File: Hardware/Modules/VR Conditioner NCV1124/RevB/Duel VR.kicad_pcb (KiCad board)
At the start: 2 copper layers, 24 x 22.4 mm, 15 parts, among them IC1 NCV1124, J3 Speedy VR Mount

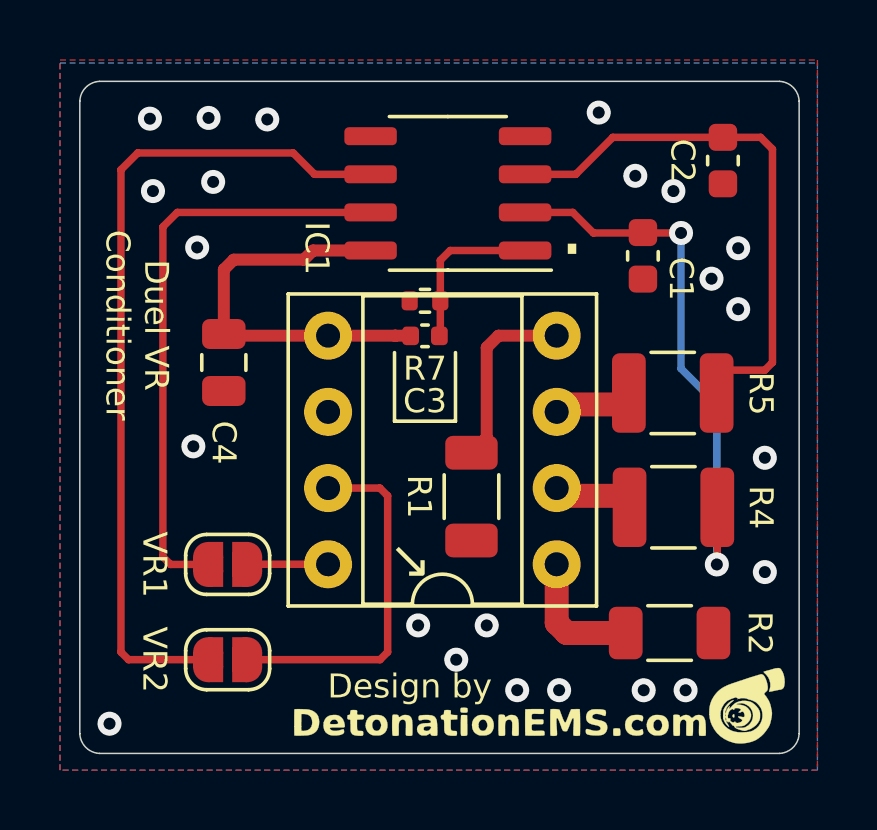
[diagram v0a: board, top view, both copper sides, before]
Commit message: VRNCV-B
Layout update. Schematic unchanged.
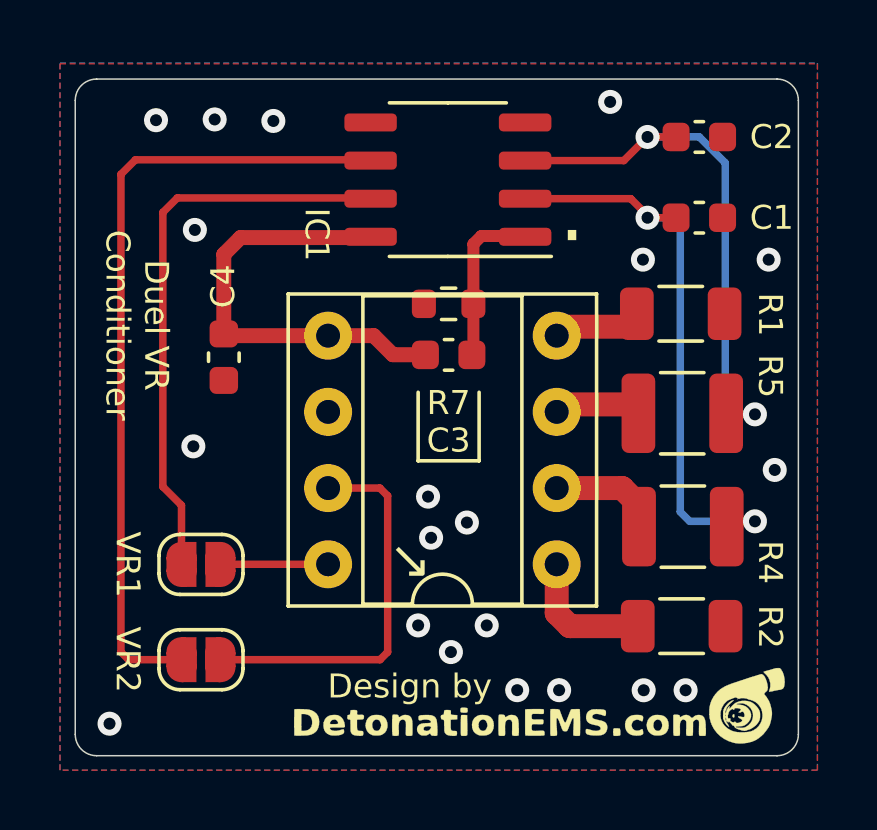
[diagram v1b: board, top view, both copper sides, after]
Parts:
- C3: footprint Capacitor_SMD:C_0402_1005Metric -> Capacitor_SMD:C_0603_1608Metric
- C4: footprint Capacitor_SMD:C_0805_2012Metric -> Capacitor_SMD:C_0603_1608Metric
- R7: footprint Resistor_SMD:R_0402_1005Metric -> Resistor_SMD:R_0603_1608Metric
- moved R1 9.26 mm to (173.2, 91.1), turned to 0 degrees
- moved C1 2.27 mm to (173.8, 87.9), turned to 180 degrees
- moved C2 1.11 mm to (173.8, 85.2), turned to 0 degrees
- moved C3 1.01 mm to (165.5, 92.5)
- moved VR1 0.89 mm to (157.2, 99.5)
- moved VR2 0.89 mm to (157.2, 102.7)
- moved R7 0.79 mm to (165.5, 90.8)
- moved R5 0.75 mm to (173.3, 94.5)
- moved R4 0.72 mm to (173.3, 98.2)
- moved R2 0.46 mm to (173.2, 101.5)
- moved IC1 0.46 mm to (165.5, 86.7)
- moved C4 0.18 mm to (158.0, 92.6)
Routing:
- net VR2-: track 6.22 -> 2.88 mm
- net Net-(IC1-OUT2): track 27.9 -> 26.5 mm
- net VDD: track 13.6 -> 14.6 mm
- net VR2OUT: track 12.1 -> 13.0 mm
- net Net-(IC1-IN2): track 17.6 -> 18.5 mm, vias 0 -> 2
- net VR1OUT: track 2.70 -> 3.58 mm
- net Net-(IC1-OUT1): track 19.7 -> 19.1 mm
- net Net-(IC1-IN1): track 18.9 -> 19.5 mm
- net GND: vias 23 -> 20
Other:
- board size 24 x 22.4 mm -> 24.1 x 22.6 mm
- board text added: "©Aaron S. 2023"
- board text removed: "©Aaron S. 2022"

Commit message: Initial upload NCV1124 RevB2
NVC1124 RevB2 upload
Ncv1124 RevB - spelling correction
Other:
- board text added: "Dual VR Conditioner"
- board text removed: "Duel VR Conditioner"
